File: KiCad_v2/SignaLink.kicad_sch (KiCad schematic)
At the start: 18 parts, among them SW1 SW_Wake, U2 ESP32-C3_SUPERMINI_TH, U3 DM-OLED096-636, U7 LTC4415IMSE_PBF

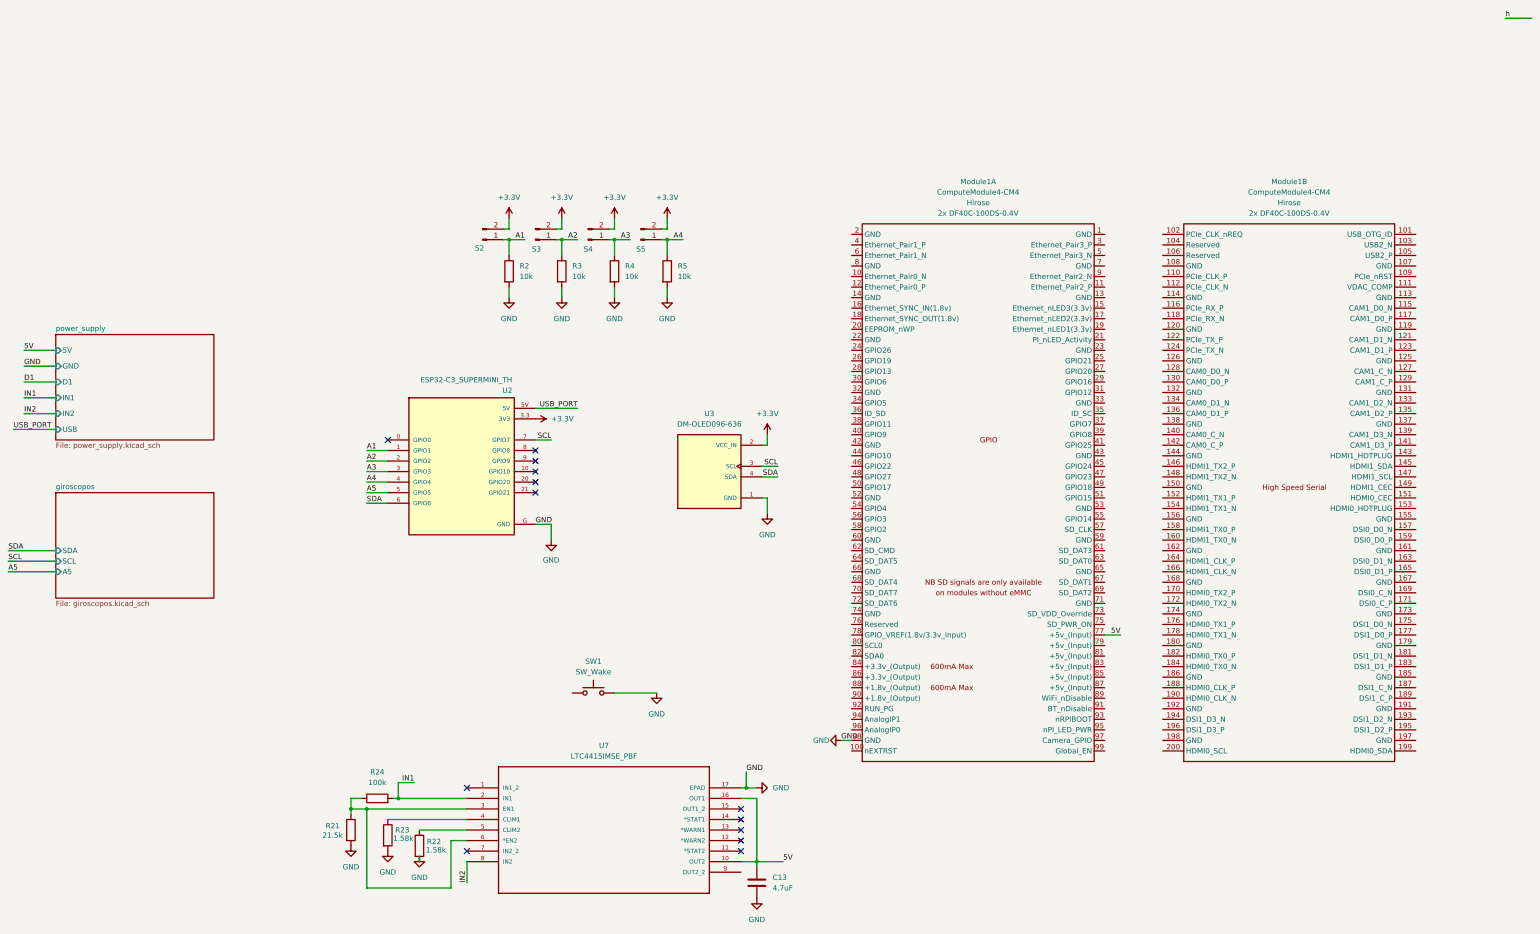
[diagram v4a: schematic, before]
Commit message: Resistencias calculadas, esquematico terminado
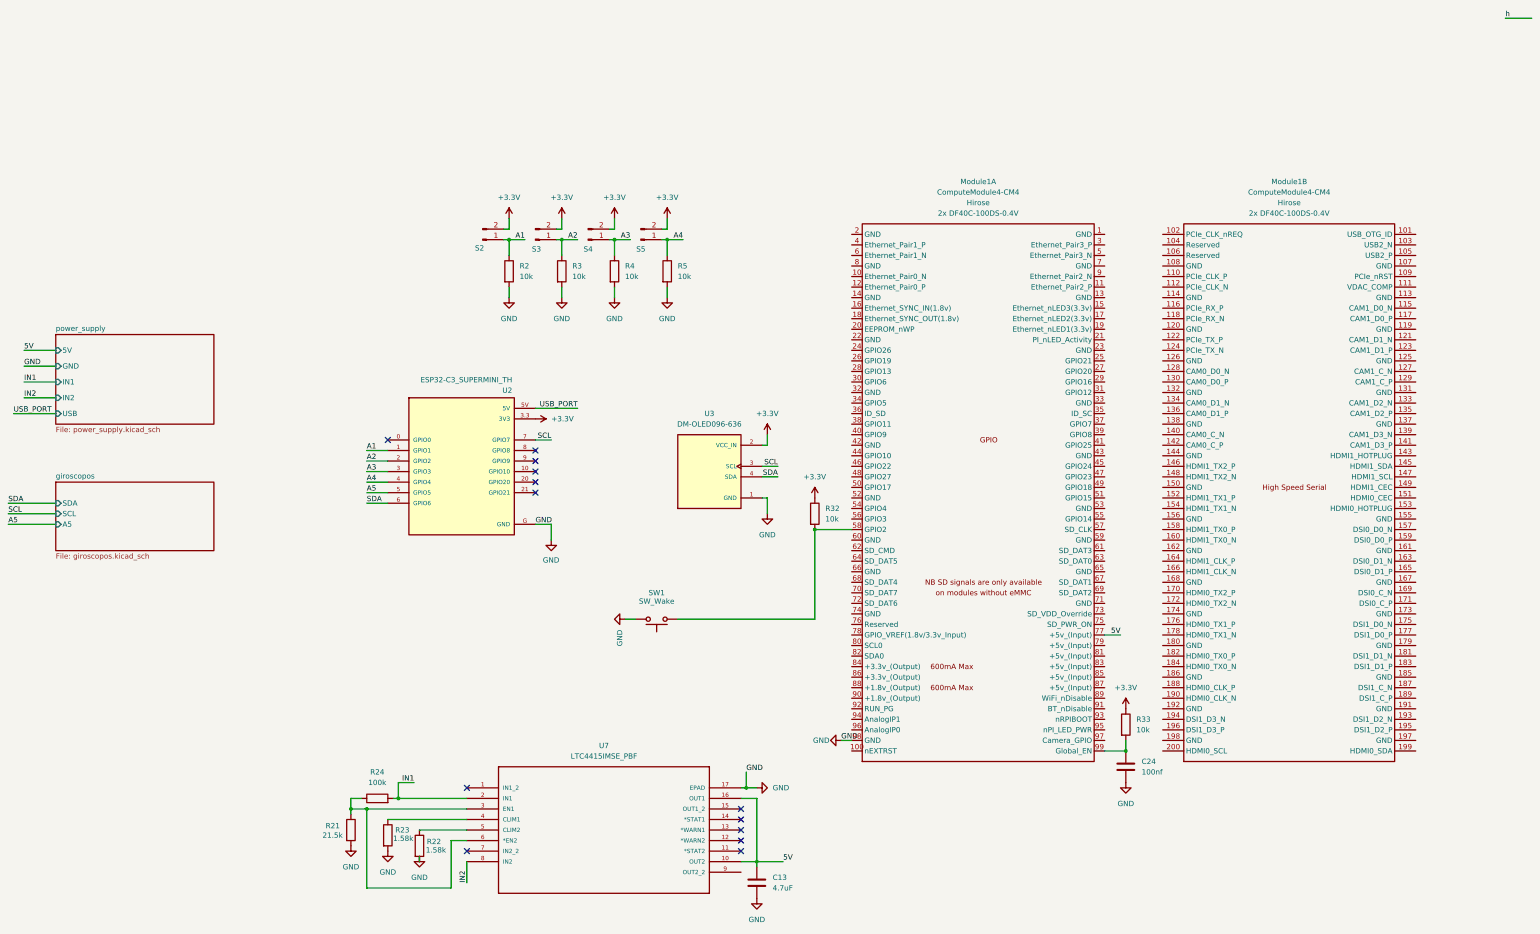
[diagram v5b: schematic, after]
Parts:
- added C24: 100nf, Capacitor_SMD:C_0603_1608Metric, symbol Device:C
- added R32, R33: 10k, Resistor_SMD:R_0603_1608Metric, symbol Device:R
- C13: footprint Capacitor_SMD:C_0805_2012Metric -> Capacitor_SMD:C_0603_1608Metric
- R2, R21, R22, R23, R24, R3, R4, R5: footprint Resistor_SMD:R_0805_2012Metric -> Resistor_SMD:R_0603_1608Metric
- SW1: footprint (none) -> Button_Switch_THT:SW_Tactile_Straight_KSA0Axx1LFTR
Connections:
- net +3.3V: now also R32.1, R33.1
- net GND: now also C24.2
- net at SW1.1: now also Module1.58 (GPIO2), R32.2
- net at Module1.99 (Global_EN): now also C24.1, R33.2
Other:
- sheet power_supply ports: added none; removed D1
- moved on the sheet: SW1

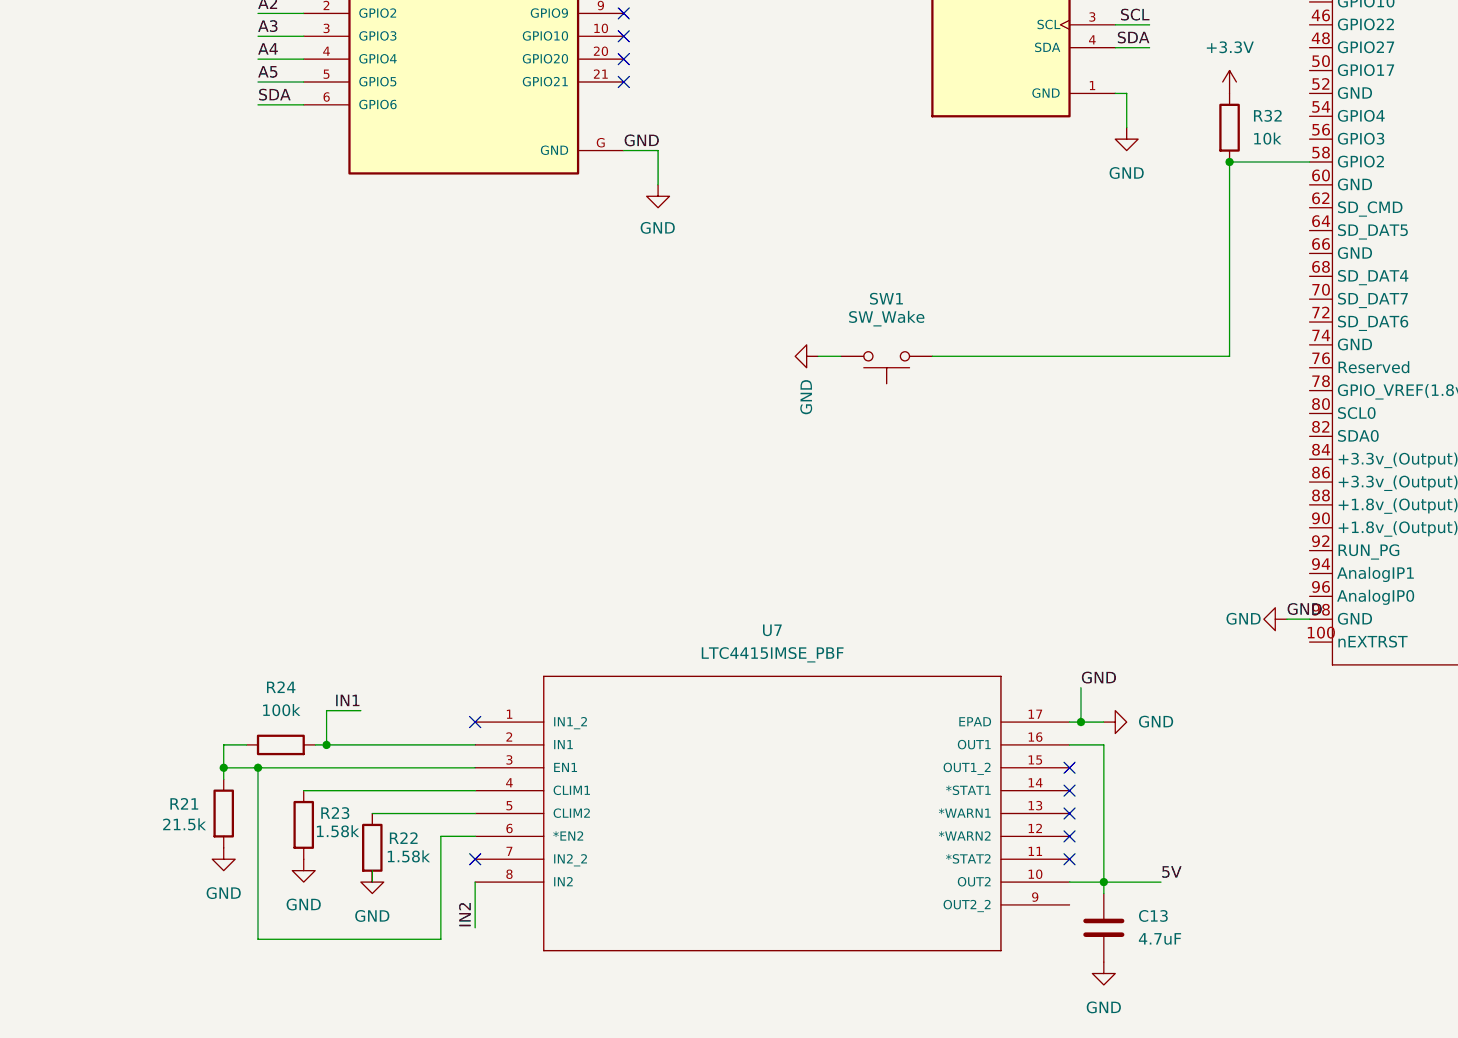
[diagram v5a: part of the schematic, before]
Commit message: agrego LT8582
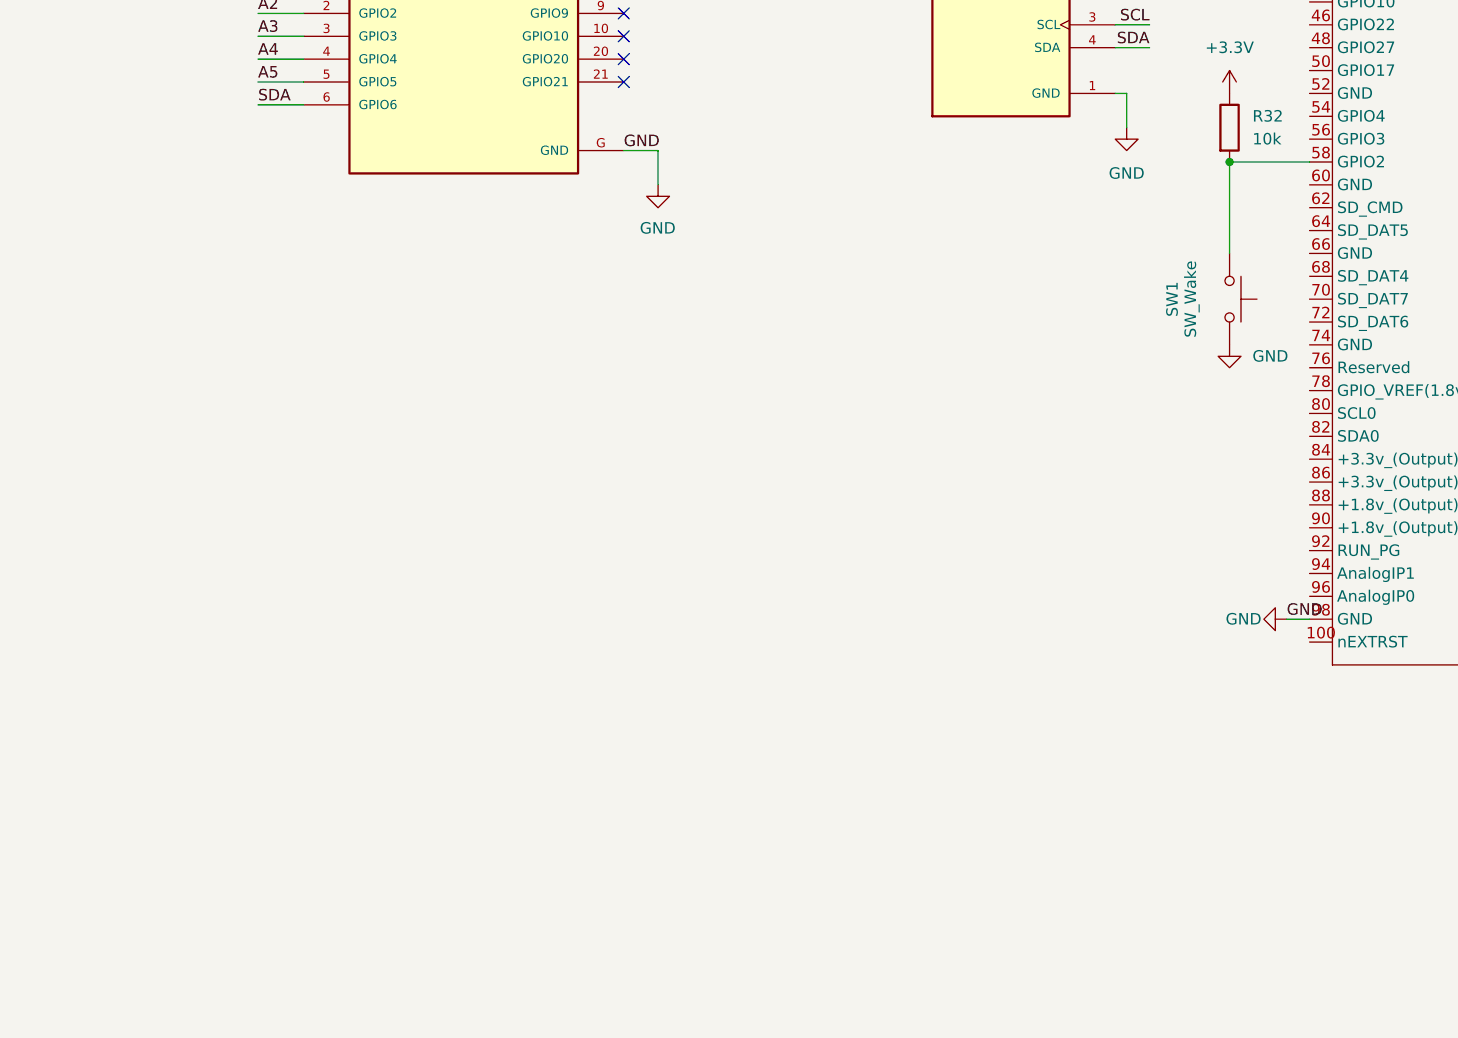
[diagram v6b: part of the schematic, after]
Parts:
- removed C13: 4.7uF, Capacitor_SMD:C_0603_1608Metric, symbol Device:C
- removed R21: 21.5k, Resistor_SMD:R_0603_1608Metric, symbol Device:R
- removed R22, R23: 1.58k, Resistor_SMD:R_0603_1608Metric, symbol Device:R
- removed R24: 100k, Resistor_SMD:R_0603_1608Metric, symbol Device:R
- removed U7: LTC4415IMSE_PBF, Custom_Footprints:MSOP-16_MSE, symbol LTC4415IMSE_PBF:LTC4415IMSE_PBF
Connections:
- no-connect marks 13 -> 6
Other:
- moved on the sheet: SW1

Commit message: circuito terminado de LT8582, falta calcular valores
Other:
- sheet power_supply ports: added none; removed IN1, IN2
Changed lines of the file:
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@@
 	(wire
 		(pts
-			(xy 120.65 90.17) (xy 121.92 90.17)
+			(xy -57.15 60.96) (xy -49.53 60.96)
 		)
 		(stroke
@@
 	(wire
 		(pts
-			(xy 139.7 148.59) (xy 142.24 148.59)
+			(xy 120.65 90.17) (xy 121.92 90.17)
 		)
 		(stroke
@@
 	(wire
 		(pts
-			(xy 120.65 77.47) (xy 121.92 77.47)
+			(xy 139.7 148.59) (xy 142.24 148.59)
 		)
 		(stroke
@@
 	(wire
 		(pts
-			(xy 85.09 27.94) (xy 83.82 27.94)
+			(xy 120.65 77.47) (xy 121.92 77.47)
 		)
 		(stroke
@@
 	(wire
 		(pts
-			(xy 299.72 -25.4) (xy 306.07 -25.4)
+			(xy 85.09 27.94) (xy 83.82 27.94)
 		)
 		(stroke
@@
 	(wire
 		(pts
-			(xy -57.15 54.61) (xy -49.53 54.61)
+			(xy 299.72 -25.4) (xy 306.07 -25.4)
 		)
 		(stroke
@@
 	(wire
 		(pts
-			(xy -49.53 66.04) (xy -57.15 66.04)
+			(xy -58.42 66.04) (xy -49.53 66.04)
 		)
 		(stroke
@@
 	(wire
 		(pts
-			(xy -59.69 69.85) (xy -49.53 69.85)
-		)
-		(stroke
-			(width 0)
-			(type default)
-		)
-	)
-	(wire
-		(pts
 			(xy 203.2 151.13) (xy 208.28 151.13)
 		)
@@
 	(wire
 		(pts
-			(xy -57.15 58.42) (xy -49.53 58.42)
-		)
-		(stroke
-			(width 0)
-			(type default)
-		)
-	)
-	(wire
-		(pts
 			(xy 96.52 27.94) (xy 97.79 27.94)
 		)
@@
 	(wire
 		(pts
+			(xy -57.15 57.15) (xy -49.53 57.15)
+		)
+		(stroke
+			(width 0)
+			(type default)
+		)
+	)
+	(wire
+		(pts
 			(xy 59.69 27.94) (xy 63.5 27.94)
 		)
@@
 		)
 	)
-	(wire
-		(pts
-			(xy -57.15 62.23) (xy -49.53 62.23)
-		)
-		(stroke
-			(width 0)
-			(type default)
-		)
-	)
 	(label "GND"
-		(at -57.15 58.42 0)
+		(at -57.15 60.96 0)
 		(effects
 			(font
@@
 		)
 	)
-	(label "IN1"
-		(at -57.15 62.23 0)
-		(effects
-			(font
-				(size 1.27 1.27)
-			)
-			(justify left bottom)
-		)
-	)
 	(label "SCL"
 		(at 69.85 76.2 180)
@@
 	)
 	(label "5V"
-		(at -57.15 54.61 0)
+		(at -57.15 57.15 0)
 		(effects
 			(font
@@
 	)
 	(label "USB_PORT"
-		(at -59.69 69.85 0)
+		(at -58.42 66.04 0)
 		(effects
 			(font
@@
 		)
 	)
-	(label "IN2"
-		(at -57.15 66.04 0)
-		(effects
-			(font
-				(size 1.27 1.27)
-			)
-			(justify left bottom)
-		)
-	)
 	(symbol
 		(lib_id "Device:R")
@@
 		)
 		(pin "5V" input
-			(at -49.53 54.61 180)
+			(at -49.53 57.15 180)
 			(effects
 				(font
@@
 		)
 		(pin "GND" input
-			(at -49.53 58.42 180)
-			(effects
-				(font
-					(size 1.27 1.27)
-				)
-				(justify left)
-			)
-		)
-		(pin "IN1" input
-			(at -49.53 62.23 180)
-			(effects
-				(font
-					(size 1.27 1.27)
-				)
-				(justify left)
-			)
-		)
-		(pin "IN2" input
-			(at -49.53 66.04 180)
+			(at -49.53 60.96 180)
 			(effects
 				(font
@@
 		)
 		(pin "USB" input
-			(at -49.53 69.85 180)
+			(at -49.53 66.04 180)
 			(effects
 				(font
